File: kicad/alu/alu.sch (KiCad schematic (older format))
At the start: 8 parts, among them J3 DB25_Male, J4 DB37_Male, U1 SN74ALVC00, U2 SN74ALVC00

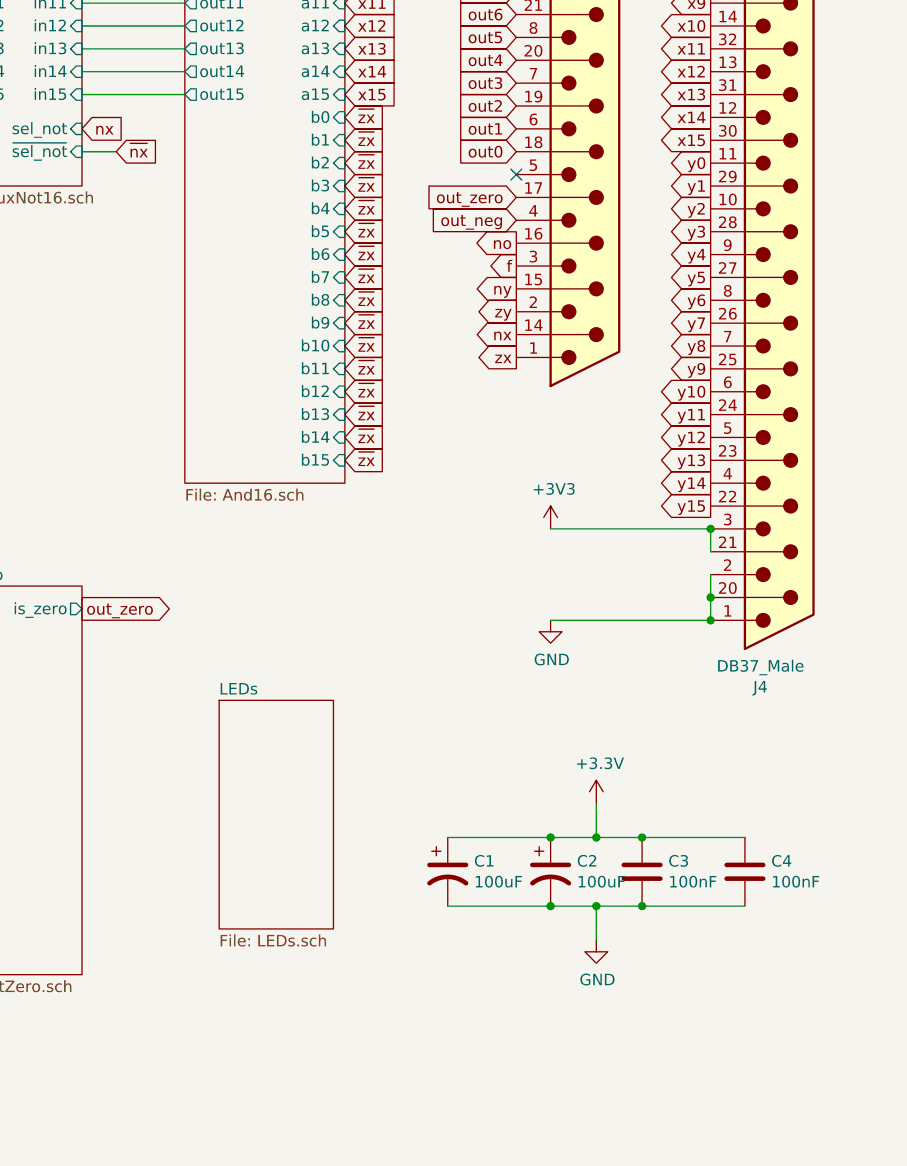
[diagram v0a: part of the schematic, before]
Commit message: ALU schematic, layout, routing complete. Associated motherboardmod. Also added Load LED to register and program counter boards.
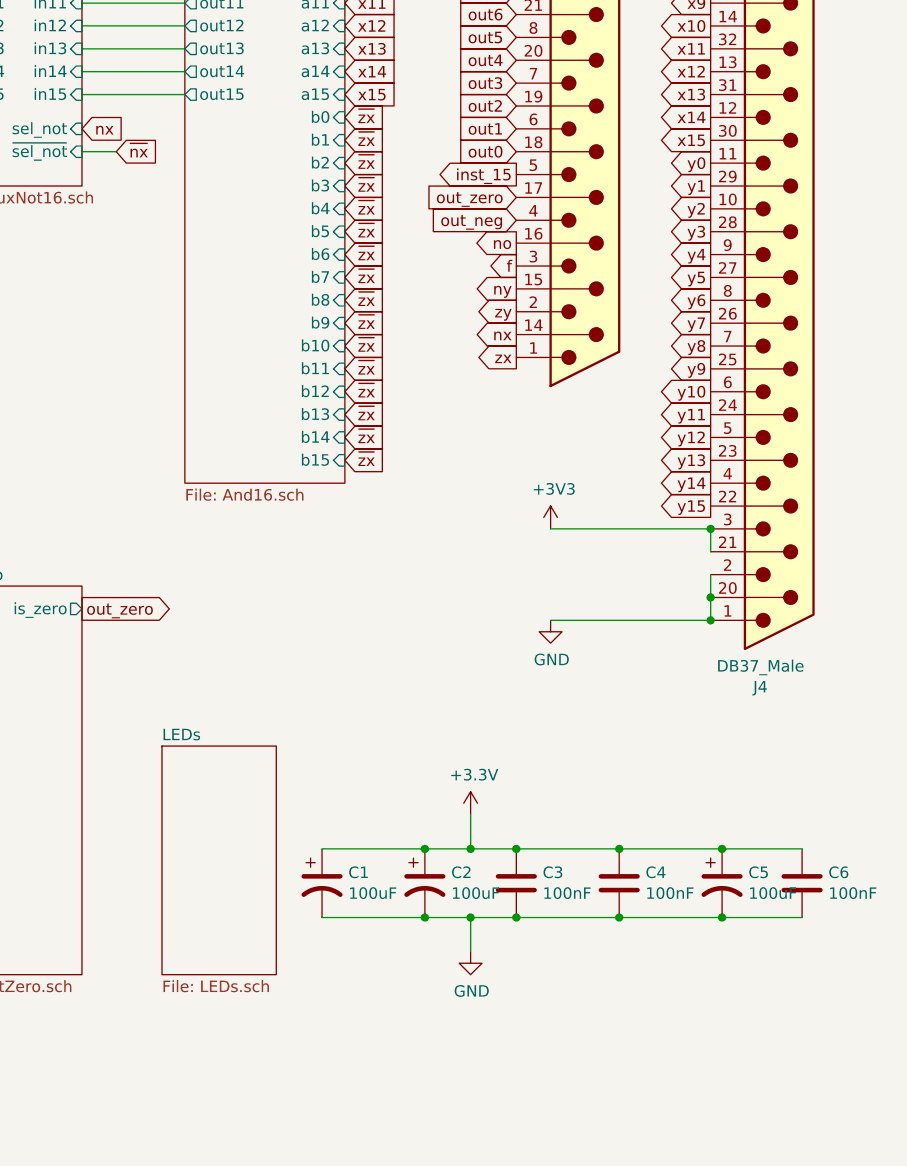
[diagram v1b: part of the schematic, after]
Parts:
- added C5: 100uF, Capacitor_THT:CP_Radial_D8.0mm_P2.50mm, symbol Device:CP1
- added C6: 100nF, Capacitor_THT:C_Disc_D5.0mm_W2.5mm_P5.00mm, symbol Device:C
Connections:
- net +3V3: now also C5.1, C6.1
- net GND: now also C5.2, C6.2
- net inst_15: now reaches J3.5
- no-connect marks 7 -> 6
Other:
- moved on the sheet: C1, C2, C3, C4
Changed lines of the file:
@@
 L Device:CP1 C2
 U 1 1 5E7D554F
-P 9900 5650
-F 0 "C2" H 10015 5696 50  0000 L CNN
-F 1 "100uF" H 10015 5605 50  0000 L CNN
-F 2 "Capacitor_THT:CP_Radial_D8.0mm_P2.50mm" H 9900 5650 50  0001 C CNN
-F 3 "~" H 9900 5650 50  0001 C CNN
-F 4 "P15797CT-ND" H 9900 5650 50  0001 C CNN "Digikey PN"
-	1    9900 5650
+P 9350 5700
+F 0 "C2" H 9465 5746 50  0000 L CNN
+F 1 "100uF" H 9465 5655 50  0000 L CNN
+F 2 "Capacitor_THT:CP_Radial_D8.0mm_P2.50mm" H 9350 5700 50  0001 C CNN
+F 3 "~" H 9350 5700 50  0001 C CNN
+F 4 "P15797CT-ND" H 9350 5700 50  0001 C CNN "Digikey PN"
+	1    9350 5700
 	1    0    0    -1
 $EndComp
@@
 L Device:C C3
 U 1 1 5E7D725F
-P 10300 5650
-F 0 "C3" H 10415 5696 50  0000 L CNN
-F 1 "100nF" H 10415 5605 50  0000 L CNN
-F 2 "Capacitor_THT:C_Disc_D5.0mm_W2.5mm_P5.00mm" H 10338 5500 50  0001 C CNN
-F 3 "~" H 10300 5650 50  0001 C CNN
-F 4 "BC5229CT-ND" H 10300 5650 50  0001 C CNN "Digikey PN"
-	1    10300 5650
+P 9750 5700
+F 0 "C3" H 9865 5746 50  0000 L CNN
+F 1 "100nF" H 9865 5655 50  0000 L CNN
+F 2 "Capacitor_THT:C_Disc_D5.0mm_W2.5mm_P5.00mm" H 9788 5550 50  0001 C CNN
+F 3 "~" H 9750 5700 50  0001 C CNN
+F 4 "BC5229CT-ND" H 9750 5700 50  0001 C CNN "Digikey PN"
+	1    9750 5700
 	1    0    0    -1
 $EndComp
@@
 L power:GND #PWR023
 U 1 1 5E7D8BF5
-P 10100 5950
-F 0 "#PWR023" H 10100 5700 50  0001 C CNN
-F 1 "GND" H 10105 5777 50  0000 C CNN
-F 2 "" H 10100 5950 50  0001 C CNN
-F 3 "" H 10100 5950 50  0001 C CNN
-	1    10100 5950
-	1    0    0    -1
-$EndComp
-Wire Wire Line
-	9900 5800 10100 5800
-Wire Wire Line
-	10100 5800 10100 5950
-Wire Wire Line
-	10300 5800 10100 5800
-Connection ~ 10100 5800
+P 9550 6000
+F 0 "#PWR023" H 9550 5750 50  0001 C CNN
+F 1 "GND" H 9555 5827 50  0000 C CNN
+F 2 "" H 9550 6000 50  0001 C CNN
+F 3 "" H 9550 6000 50  0001 C CNN
+	1    9550 6000
+	1    0    0    -1
+$EndComp
+Wire Wire Line
+	9350 5850 9550 5850
+Wire Wire Line
+	9550 5850 9550 6000
+Wire Wire Line
+	9750 5850 9550 5850
+Connection ~ 9550 5850
 $Comp
 L power:+3.3V #PWR022
 U 1 1 5E7E5BC1
-P 10100 5350
-F 0 "#PWR022" H 10100 5200 50  0001 C CNN
-F 1 "+3.3V" H 10115 5523 50  0000 C CNN
-F 2 "" H 10100 5350 50  0001 C CNN
-F 3 "" H 10100 5350 50  0001 C CNN
-	1    10100 5350
-	1    0    0    -1
-$EndComp
-Wire Wire Line
-	9900 5500 10100 5500
-Wire Wire Line
-	10300 5500 10100 5500
-Connection ~ 10100 5500
-Wire Wire Line
-	10100 5500 10100 5350
+P 9550 5400
+F 0 "#PWR022" H 9550 5250 50  0001 C CNN
+F 1 "+3.3V" H 9565 5573 50  0000 C CNN
+F 2 "" H 9550 5400 50  0001 C CNN
+F 3 "" H 9550 5400 50  0001 C CNN
+	1    9550 5400
+	1    0    0    -1
+$EndComp
+Wire Wire Line
+	9350 5550 9550 5550
+Wire Wire Line
+	9750 5550 9550 5550
+Connection ~ 9550 5550
+Wire Wire Line
+	9550 5550 9550 5400
 $Comp
 L Connector:DB37_Male J4
@@
 L Device:CP1 C1
 U 1 1 5E8C36BA
-P 9450 5650
-F 0 "C1" H 9565 5696 50  0000 L CNN
-F 1 "100uF" H 9565 5605 50  0000 L CNN
-F 2 "Capacitor_THT:CP_Radial_D8.0mm_P2.50mm" H 9450 5650 50  0001 C CNN
-F 3 "~" H 9450 5650 50  0001 C CNN
-F 4 "P15797CT-ND" H 9450 5650 50  0001 C CNN "Digikey PN"
-	1    9450 5650
+P 8900 5700
+F 0 "C1" H 9015 5746 50  0000 L CNN
+F 1 "100uF" H 9015 5655 50  0000 L CNN
+F 2 "Capacitor_THT:CP_Radial_D8.0mm_P2.50mm" H 8900 5700 50  0001 C CNN
+F 3 "~" H 8900 5700 50  0001 C CNN
+F 4 "P15797CT-ND" H 8900 5700 50  0001 C CNN "Digikey PN"
+	1    8900 5700
 	1    0    0    -1
 $EndComp
@@
 L Device:C C4
 U 1 1 5E8C3C3C
-P 10750 5650
-F 0 "C4" H 10865 5696 50  0000 L CNN
-F 1 "100nF" H 10865 5605 50  0000 L CNN
-F 2 "Capacitor_THT:C_Disc_D5.0mm_W2.5mm_P5.00mm" H 10788 5500 50  0001 C CNN
-F 3 "~" H 10750 5650 50  0001 C CNN
-F 4 "BC5229CT-ND" H 10750 5650 50  0001 C CNN "Digikey PN"
-	1    10750 5650
-	1    0    0    -1
-$EndComp
-Wire Wire Line
-	9450 5500 9900 5500
-Connection ~ 9900 5500
-Wire Wire Line
-	9450 5800 9900 5800
-Connection ~ 9900 5800
-Wire Wire Line
-	10750 5800 10300 5800
-Connection ~ 10300 5800
-Wire Wire Line
-	10300 5500 10750 5500
-Connection ~ 10300 5500
+P 10200 5700
+F 0 "C4" H 10315 5746 50  0000 L CNN
+F 1 "100nF" H 10315 5655 50  0000 L CNN
+F 2 "Capacitor_THT:C_Disc_D5.0mm_W2.5mm_P5.00mm" H 10238 5550 50  0001 C CNN
+F 3 "~" H 10200 5700 50  0001 C CNN
+F 4 "BC5229CT-ND" H 10200 5700 50  0001 C CNN "Digikey PN"
+	1    10200 5700
+	1    0    0    -1
+$EndComp
+Wire Wire Line
+	8900 5550 9350 5550
+Connection ~ 9350 5550
+Wire Wire Line
+	8900 5850 9350 5850
+Connection ~ 9350 5850
+Wire Wire Line
+	10200 5850 9750 5850
+Connection ~ 9750 5850
+Wire Wire Line
+	9750 5550 10200 5550
+Connection ~ 9750 5550
 Wire Wire Line
 	10600 4250 10600 4150
@@
 Text GLabel 9750 2700 0    50   Input ~ 0
 out_zero
-NoConn ~ 9750 2600
 Text GLabel 9000 750  2    50   Input ~ 0
 x0
@@
 xplusy_15
 $Sheet
-S 8450 4900 500  1000
+S 8200 5100 500  1000
 U 5ED91E72
 F0 "LEDs" 50
 F1 "LEDs.sch" 50
 $EndSheet
+Text GLabel 9750 2600 0    50   Output ~ 0
+inst_15
+$Comp
+L Device:CP1 C5
+U 1 1 5EA04B1D
+P 10650 5700
+F 0 "C5" H 10765 5746 50  0000 L CNN
+F 1 "100uF" H 10765 5655 50  0000 L CNN
+F 2 "Capacitor_THT:CP_Radial_D8.0mm_P2.50mm" H 10650 5700 50  0001 C CNN
+F 3 "~" H 10650 5700 50  0001 C CNN
+F 4 "P15797CT-ND" H 10650 5700 50  0001 C CNN "Digikey PN"
+	1    10650 5700
+	1    0    0    -1
+$EndComp
+$Comp
+L Device:C C6
+U 1 1 5EA099FE
+P 11000 5700
+F 0 "C6" H 11115 5746 50  0000 L CNN
+F 1 "100nF" H 11115 5655 50  0000 L CNN
+F 2 "Capacitor_THT:C_Disc_D5.0mm_W2.5mm_P5.00mm" H 11038 5550 50  0001 C CNN
+F 3 "~" H 11000 5700 50  0001 C CNN
+F 4 "BC5229CT-ND" H 11000 5700 50  0001 C CNN "Digikey PN"
+	1    11000 5700
+	1    0    0    -1
+$EndComp
+Wire Wire Line
+	10200 5550 10650 5550
+Connection ~ 10200 5550
+Connection ~ 10650 5550
+Wire Wire Line
+	10650 5550 11000 5550
+Wire Wire Line
+	10200 5850 10650 5850
+Connection ~ 10200 5850
+Connection ~ 10650 5850
+Wire Wire Line
+	10650 5850 11000 5850
 $EndSCHEMATC

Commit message: Readme updates (#6)
* Readme intro section

* Board revisions for manufacturing, add digikey PNs to all, added logo.
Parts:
- J3: footprint Connector_Dsub:DSUB-25_Male_Horizontal_P2.77x2.84mm_EdgePinOffset4.94mm_Housed_MountingHolesOffset7.48mm -> Connector_Dsub:DSUB-25_Male_Horizontal_P2.77x2.84mm_EdgePinOffset7.70mm_Housed_MountingHolesOffset9.12mm; Digikey PN (none) -> AE10980-ND
- J4: footprint Connector_Dsub:DSUB-37_Male_Horizontal_P2.77x2.84mm_EdgePinOffset4.94mm_Housed_MountingHolesOffset7.48mm -> Connector_Dsub:DSUB-37_Male_Horizontal_P2.77x2.84mm_EdgePinOffset7.70mm_Housed_MountingHolesOffset9.12mm; Digikey PN (none) -> AE10986-ND
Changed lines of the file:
@@
 F 0 "J4" H 10818 658 50  0000 C CNN
 F 1 "DB37_Male" H 10818 749 50  0000 C CNN
-F 2 "Connector_Dsub:DSUB-37_Male_Horizontal_P2.77x2.84mm_EdgePinOffset4.94mm_Housed_MountingHolesOffset7.48mm" H 10900 2750 50  0001 C CNN
+F 2 "Connector_Dsub:DSUB-37_Male_Horizontal_P2.77x2.84mm_EdgePinOffset7.70mm_Housed_MountingHolesOffset9.12mm" H 10900 2750 50  0001 C CNN
 F 3 " ~" H 10900 2750 50  0001 C CNN
+F 4 "AE10986-ND" H 10900 2750 50  0001 C CNN "Digikey PN"
 	1    10900 2750
 	1    0    0    -1
@@
 F 0 "J3" H 10000 3750 50  0000 L CNN
 F 1 "DB25_Male" H 9950 3650 50  0000 L CNN
-F 2 "Connector_Dsub:DSUB-25_Male_Horizontal_P2.77x2.84mm_EdgePinOffset4.94mm_Housed_MountingHolesOffset7.48mm" H 10050 2200 50  0001 C CNN
+F 2 "Connector_Dsub:DSUB-25_Male_Horizontal_P2.77x2.84mm_EdgePinOffset7.70mm_Housed_MountingHolesOffset9.12mm" H 10050 2200 50  0001 C CNN
 F 3 " ~" H 10050 2200 50  0001 C CNN
+F 4 "AE10980-ND" H 10050 2200 50  0001 C CNN "Digikey PN"
 	1    10050 2200
 	1    0    0    -1
